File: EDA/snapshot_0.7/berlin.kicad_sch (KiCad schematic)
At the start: 754 parts, among them J201 TYPE-C-31-M12_13, J202 Conn_ARM_JTAG_SWD_10, J203 LCDCON, Q701 DTC123J, SW1,1 Rotary_Encoder_Switch_Chassis, SW1,10 MXSwitch, SW1,11 MXSwitch, SW1,12 MXSwitch, SW1,13 MXSwitch, SW1,14 MXSwitch, SW1,15 MXSwitch, SW1,16 Rotary_Encoder_Switch_Chassis, SW1,2 MXSwitch, SW1,3 MXSwitch, SW1,4 MXSwitch, SW1,5 MXSwitch, SW1,6 MXSwitch, SW1,7 MXSwitch, SW1,8 MXSwitch, SW1,9 MXSwitch, SW2,1 MXSwitch, SW2,10 MXSwitch, SW2,11 MXSwitch, SW2,12 MXSwitch, SW2,13 MXSwitch, SW2,14 MXSwitch, SW2,15 MXSwitch, SW2,16 MXSwitch, SW2,17 MXSwitch, SW2,18 MXSwitch, SW2,19 MXSwitch, SW2,2 MXSwitch, SW2,3 MXSwitch, SW2,4 MXSwitch, SW2,5 MXSwitch, SW2,6 MXSwitch, SW2,7 MXSwitch, SW2,9 MXSwitch, SW201 SW_Push, SW3,1 MXSwitch, SW3,10 MXSwitch, SW3,11 MXSwitch, SW3,12 MXSwitch, SW3,13 MXSwitch, SW3,14 MXSwitch, SW3,15 MXSwitch, SW3,16 MXSwitch, SW3,17 MXSwitch, SW3,18 MXSwitch, SW3,19 MXSwitch, SW3,2 MXSwitch, SW3,3 MXSwitch, SW3,4 MXSwitch, SW3,5 MXSwitch, SW3,6 MXSwitch, SW3,7 MXSwitch, SW3,8 MXSwitch, SW3,9 MXSwitch, SW4,1 MXSwitch, SW4,10 MXSwitch, SW4,11 MXSwitch, SW4,12 MXSwitch, SW4,13 MXSwitch, SW4,14 MXSwitch, SW4,15 MXSwitch, SW4,16 MXSwitch, SW4,17 MXSwitch, SW4,18 MXSwitch, SW4,19 MXSwitch, SW4,2 MXSwitch, SW4,3 MXSwitch, SW4,4 MXSwitch, SW4,5 MXSwitch, SW4,6 MXSwitch, SW4,7 MXSwitch, SW4,8 MXSwitch, SW4,9 MXSwitch, SW5,1 MXSwitch, SW5,10 MXSwitch, SW5,11 MXSwitch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

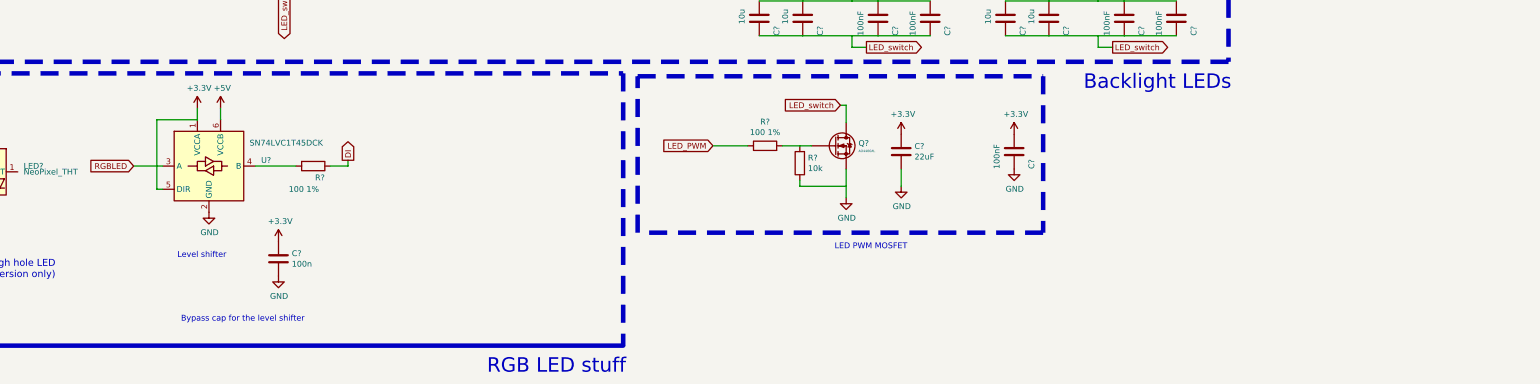
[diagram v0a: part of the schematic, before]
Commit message: add sn74 and bug fixes
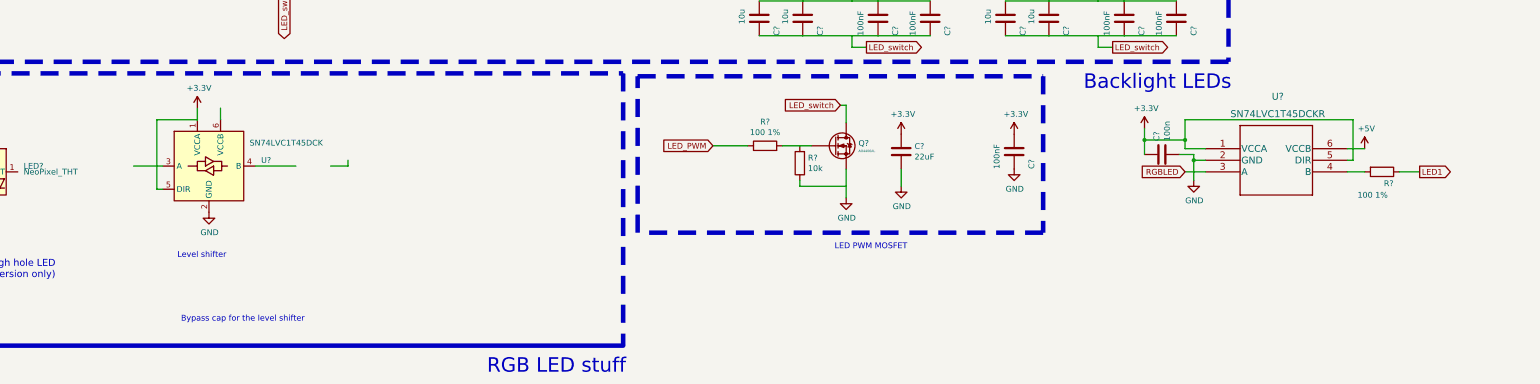
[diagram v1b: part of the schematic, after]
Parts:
- added U?: SN74LVC1T45DCKR, DCK6, symbol 2022-06-09_13-57-10:SN74LVC1T45DCKR
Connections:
- net +3V3: now also U?.1 (VCCA), U?.5 (DIR)
- net +5V: now also U?.6 (VCCB); no longer U?.6 (VCCB)
- net DI: no longer R?.1
- net GND: now also U?.2 (GND)
- net LED1: now also R?.1
- net RGBLED: now also U?.3 (A); no longer U?.3 (A)
- net at R?.2: now also U?.4 (B); no longer U?.4 (B)
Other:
- moved on the sheet: C?, R?

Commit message: update mcu connections for potentiometers and rgb leds
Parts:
- gave numbers to parts that had none: 6
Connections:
- net +3V3: no longer U?.1 (VCCA), U?.5 (DIR)
- net GND: no longer U?.2 (GND)
- net PV1: now also U501.25 (PA2)
- net PV2: now also U501.24 (PA1)
- net PV3: now also U501.23 (PA0)
- net RGBLED: now also U501.55 (PD8)
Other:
- moved on the sheet: U?

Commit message: add lock led & rot enc conns & make parity test ready
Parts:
- removed C? (x15): 10u, Capacitor_SMD:C_1206_3216Metric_Pad1.42x1.75mm_HandSolder, symbol Device:C
- removed C? (x26): 100nF, Capacitor_SMD:C_0805_2012Metric_Pad1.15x1.40mm_HandSolder, symbol Device:C
- removed C?: 22uF, Capacitor_SMD:C_1206_3216Metric_Pad1.42x1.75mm_HandSolder, symbol Device:C
- removed C?: 100n, Capacitor_SMD:C_0805_2012Metric_Pad1.15x1.40mm_HandSolder, symbol Device:C
- removed LED? (x140): LED, LED_THT:LED_D3.0mm_Clear, symbol Device:LED
- removed LED?: NeoPixel_THT, LED_THT:LED_D5.0mm-4_RGB, symbol LED:NeoPixel_THT
- removed Q?: AO4406AL, acheronComponents:SOIC-8, symbol Boston-controller-STM32-rescue:AO4406AL-Acheron
- removed R? (x134): 100 1%, Resistor_SMD:R_0805_2012Metric_Pad1.15x1.40mm_HandSolder, symbol Device:R
- removed R? (x3): 330, Resistor_THT:R_Axial_DIN0207_L6.3mm_D2.5mm_P7.62mm_Horizontal, symbol Device:R
- removed R? (x3): 10k, Resistor_SMD:R_0805_2012Metric_Pad1.15x1.40mm_HandSolder, symbol Device:R
- removed U502: SN74LVC1T45DCKR, DCK6, symbol 2022-06-09_13-57-10:SN74LVC1T45DCKR
- added R302, R303, R304, R305: 10k, Resistor_SMD:R_0805_2012Metric_Pad1.15x1.40mm_HandSolder, symbol Device:R
- added R306, R307, R308: 330, Resistor_THT:R_Axial_DIN0207_L6.3mm_D2.5mm_P7.62mm_Horizontal, symbol Device:R
- gave numbers to parts that had none: 12
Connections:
- net +3V3: now also C712.2, U502.1 (VCCA), U502.5 (DIR), R302.2, R303.2, R304.2, R305.2; no longer C1003.1, C712.1
- net +5V: now also U502.6 (VCCB); no longer C1001.1, C1002.1
- net CAP_INDICATOR: now also R307.2
- net Enc1A: now also U501.62 (PD15), R302.1
- net Enc1B: now also U501.61 (PD14), R303.1
- net Enc2A: now also U501.87 (PD6), R304.1
- net Enc2B: now also U501.88 (PD7), R305.1
- net GND: now also C712.1, U502.2 (GND); no longer C1001.2, C1002.2, C712.2
- net NUM_INDICATOR: now also R306.2
- net RGBLED: now also U502.3 (A)
- net SCRL_INDICATOR: now also R308.2
- net at R301.2: now also U502.4 (B)
- net at U501.81 (PD0): now also R306.1
- net at U501.82 (PD1): now also R307.1
- net at U501.83 (PD2): now also R308.1
- net LED_switch: no longer names the net of C1003.2
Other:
- note added: "Component annotation keys: Type Shortcut+Usage Number+Part number(max. 100 parts) Usage Number: 1-Auxiliary components for matrix 2-interface components 3-auxiliary components for logic (e.g. pullups) 5-logic/ic components 7-power delivery components 10-not yet implemented notes: components inside the matrix layout are assigned [type]+[row],[column] diodes in the matrix are labelled iteratively b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"
- note added: "LED Logic Level Shifter"
- note removed: "5mm through hole LED (3D-printed version only)"
- note removed: "Bulk caps"
- note removed: "Bypass cap for the level shifter"
- note removed: "Component annotation keys: Type Shortcut+Usage Number+Part number(max. 100 parts) Usage Number: 1-Auxiliary components for matrix 2-interface components 3-auxiliary components for logic (e.g. pullups) 5-logic/ic components 7-power delivery components notes: components inside the matrix layout are assigned [type]+[row],[column] diodes in the matrix are labelled iteratively because of sheer numbers"
- note removed: "LED PWM MOSFET"
- note removed: "Level shifter"
- note removed: "RGB LED stuff"
- moved on the sheet: C1001, C1002, C1003, C101, C102, C712, LED1,1, LED1,10, LED1,11, LED1,12, LED1,13, LED1,14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

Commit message: mitigate ~500 parity and other errors
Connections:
- net Col1: now also U501.69 (PA10); no longer U501.65 (PC8)
- net Col2: now also U501.68 (PA9); no longer U501.66 (PC9)
- net Col4: now also U501.66 (PC9); no longer U501.68 (PA9)
- net Col5: now also U501.65 (PC8); no longer U501.69 (PA10)
- net Row4: now also D92.1 (K)
- net Row5: now also D93.1 (K); no longer D92.1 (K)
- net Row6: no longer D93.1 (K)
- net C102-Pad1: now reaches C102.1, LED1,16.8 (VDD), R102.2
- net CC1: now reaches J201.A5 (CC1), R705.2
- net CC2: now reaches J201.B5 (CC2), R706.1
- net SW: now reaches C703.2, L701.1, U702.5 (SW)
- net BST: now reaches C703.1, U702.6 (BST)
- net C101-Pad1: now reaches C101.1, LED1,1.8 (VDD), R101.2

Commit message: upd .7 w/ last logic routing
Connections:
- net 1,1 INTERRUPT: now also U501.56 (PD9); no longer SW1,16.3 (SW)
- net 1,16 INTERRUPT: now reaches U501.5 (PE6)
- net 1,16 INTERRUPT: now also SW1,16.3 (SW)
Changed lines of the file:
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@@
     )
   )
-  (global_label "1,1 INTERRUPT" (shape bidirectional) (at 596.9 63.5 180) (fields_autoplaced)
-    (effects (font (size 1.27 1.27)) (justify right))
-    (property "Intersheet References" "${INTERSHEET_REFS}" (id 0) (at 580.3355 63.4206 0)
+  (global_label "1,16 INTERRUPT" (shape bidirectional) (at 596.9 63.5 180) (fields_autoplaced)
+    (effects (font (size 1.27 1.27)) (justify right))
+    (property "Intersheet References" "${INTERSHEET_REFS}" (id 0) (at 579.1259 63.4206 0)
       (effects (font (size 1.27 1.27)) (justify right) hide)
     )
@@
     (property "Intersheet References" "${INTERSHEET_REFS}" (id 0) (at 1.27 22.86 0)
       (effects (font (size 1.27 1.27)) hide)
+    )
+  )
+  (global_label "1,1 INTERRUPT" (shape bidirectional) (at 801.37 285.75 180) (fields_autoplaced)
+    (effects (font (size 1.27 1.27)) (justify right))
+    (property "Intersheet References" "${INTERSHEET_REFS}" (id 0) (at 784.8055 285.6706 0)
+      (effects (font (size 1.27 1.27)) (justify right) hide)
     )
   )
@@
     )
   )
+  (global_label "1,16 INTERRUPT" (shape bidirectional) (at 801.37 234.95 180) (fields_autoplaced)
+    (effects (font (size 1.27 1.27)) (justify right))
+    (property "Intersheet References" "${INTERSHEET_REFS}" (id 0) (at 783.5959 234.8706 0)
+      (effects (font (size 1.27 1.27)) (justify right) hide)
+    )
+  )

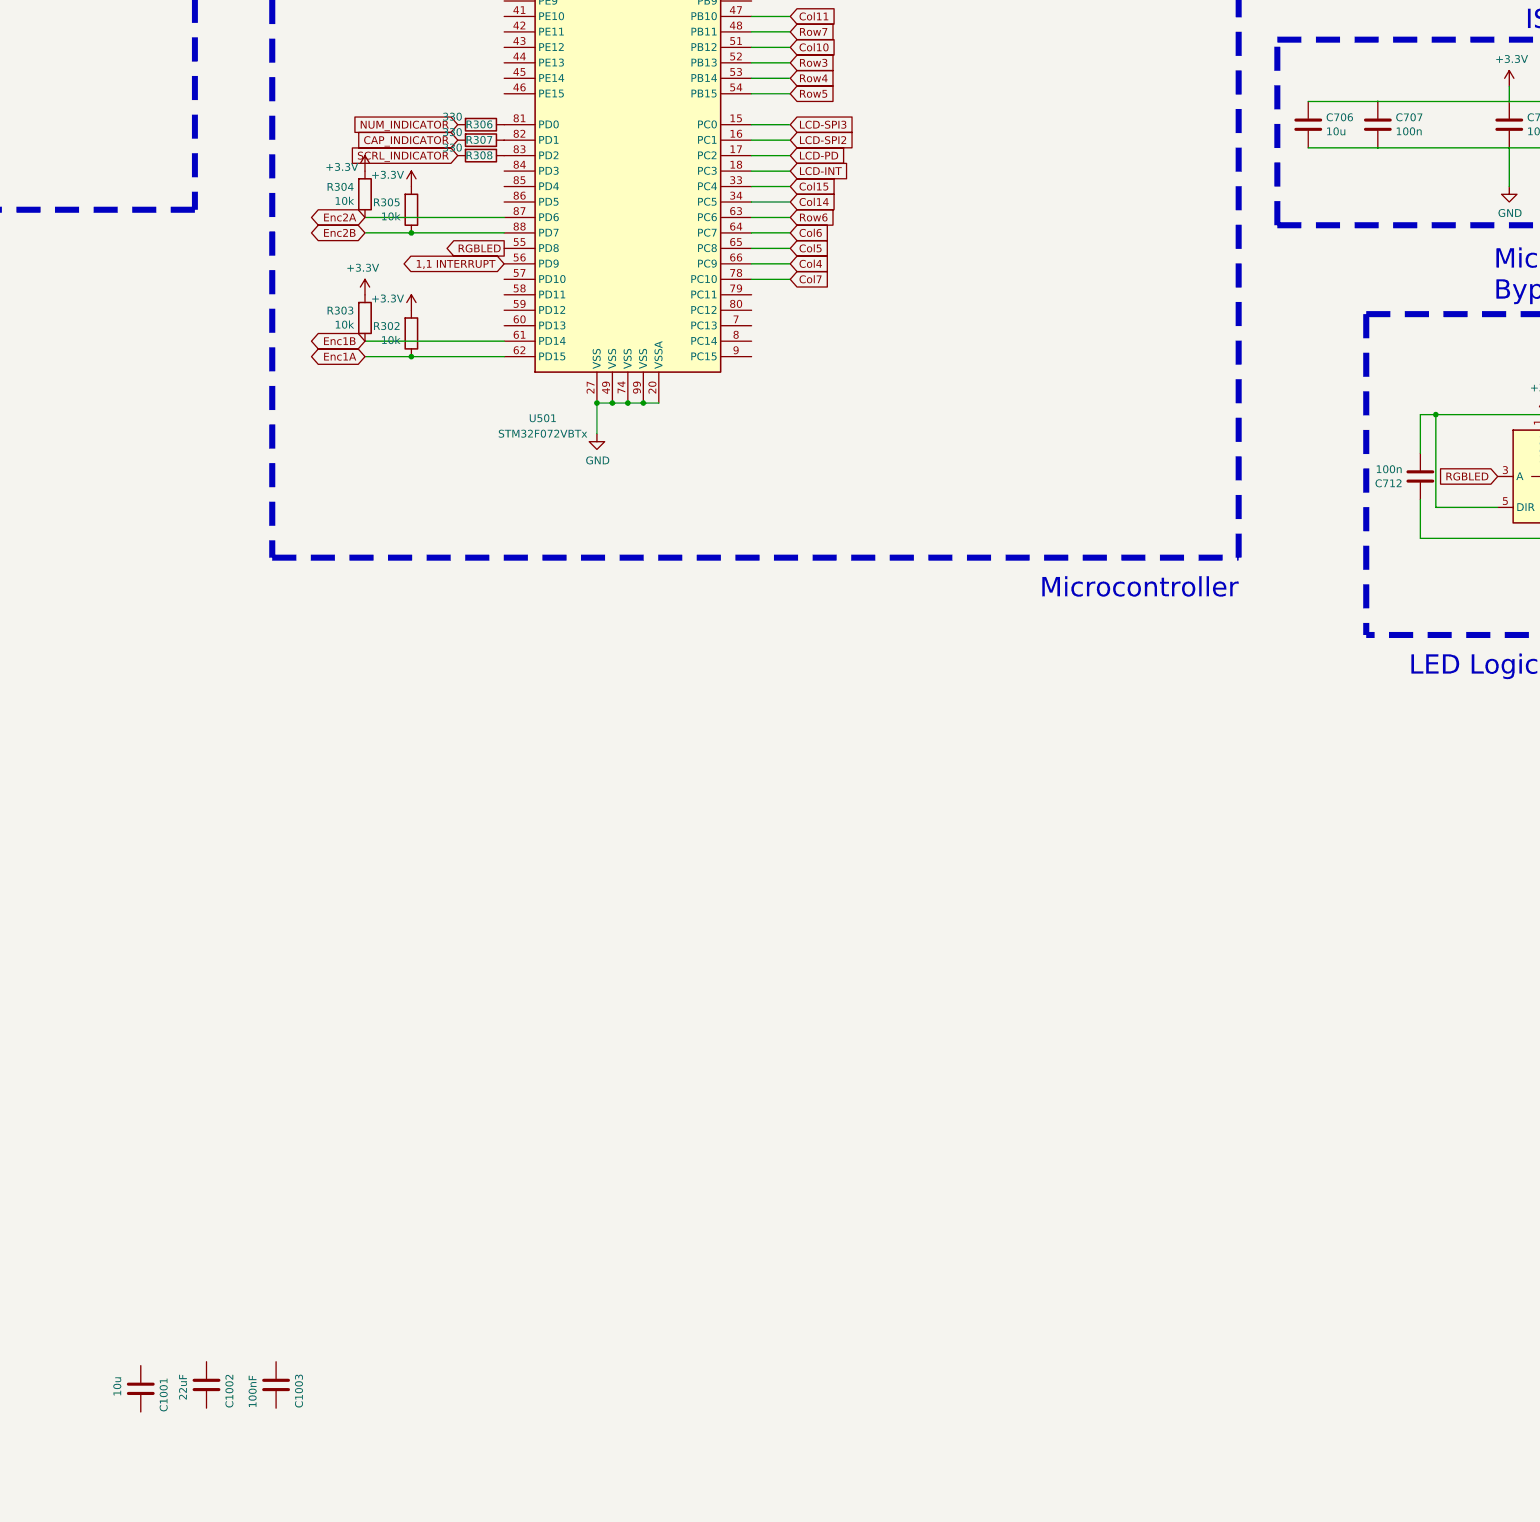
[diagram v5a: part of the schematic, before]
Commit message: 0.7: add power caps&footprints
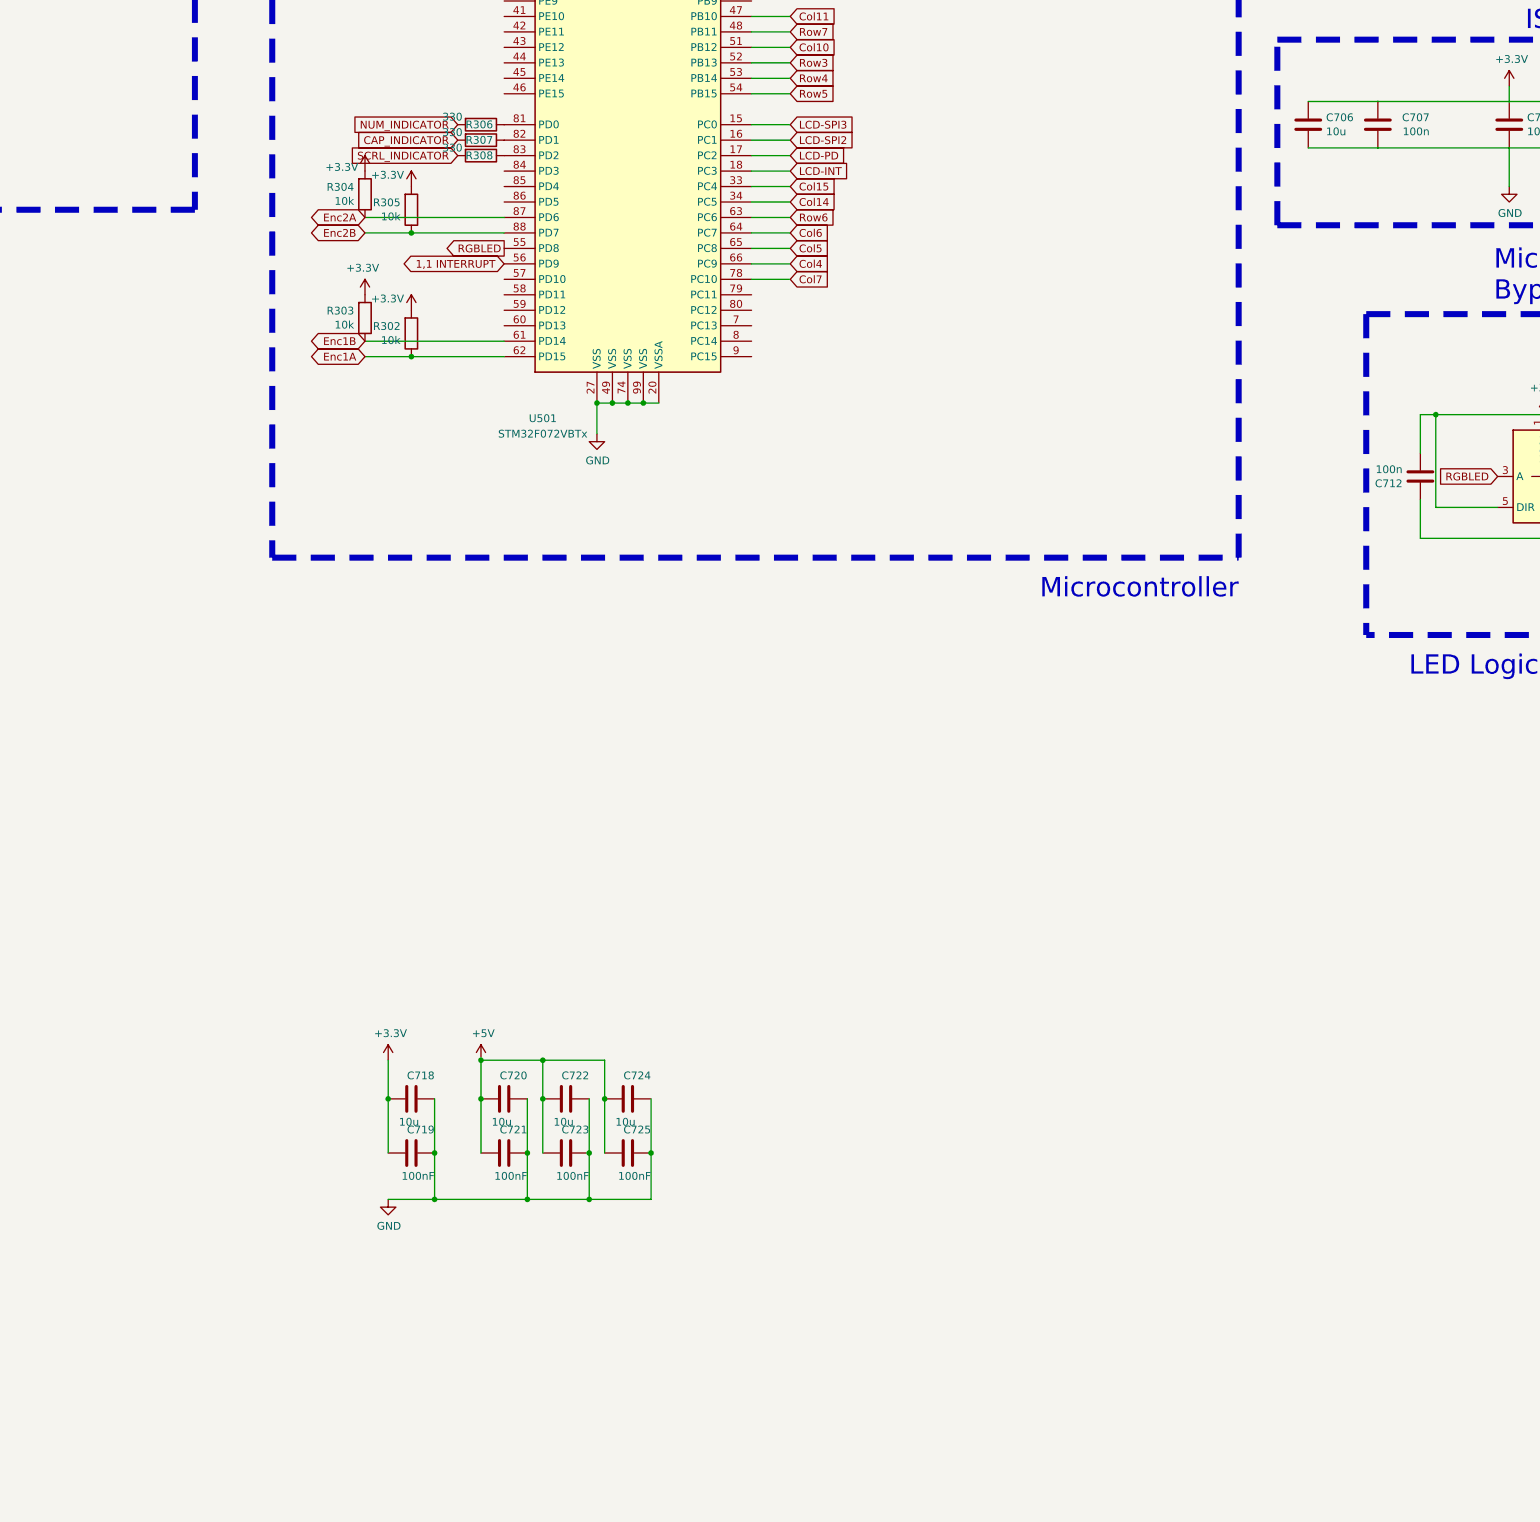
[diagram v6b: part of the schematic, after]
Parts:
- removed C1002: 22uF, Capacitor_SMD:C_1206_3216Metric_Pad1.42x1.75mm_HandSolder, symbol Device:C
- added C720, C722, C724: 10u, Capacitor_SMD:C_1206_3216Metric_Pad1.42x1.75mm_HandSolder, symbol Device:C
- added C721, C723, C725: 100nF, Capacitor_SMD:C_0805_2012Metric_Pad1.15x1.40mm_HandSolder, symbol Device:C
- renumbered C1001 to C718, C1003 to C719
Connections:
- net +3V3: now also C718.1, C719.1
- net +5V: now also C720.1, C721.1, C722.1, C723.1, C724.1, C725.1
- net GND: now also C718.2, C719.2, C720.2, C721.2, C722.2, C723.2, C724.2, C725.2
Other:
- moved on the sheet: C718, C719
